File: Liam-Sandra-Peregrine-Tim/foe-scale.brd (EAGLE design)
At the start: 96.2 x 67.3 mm, 49 parts, among them U1 LM311, U2 SAMD21E

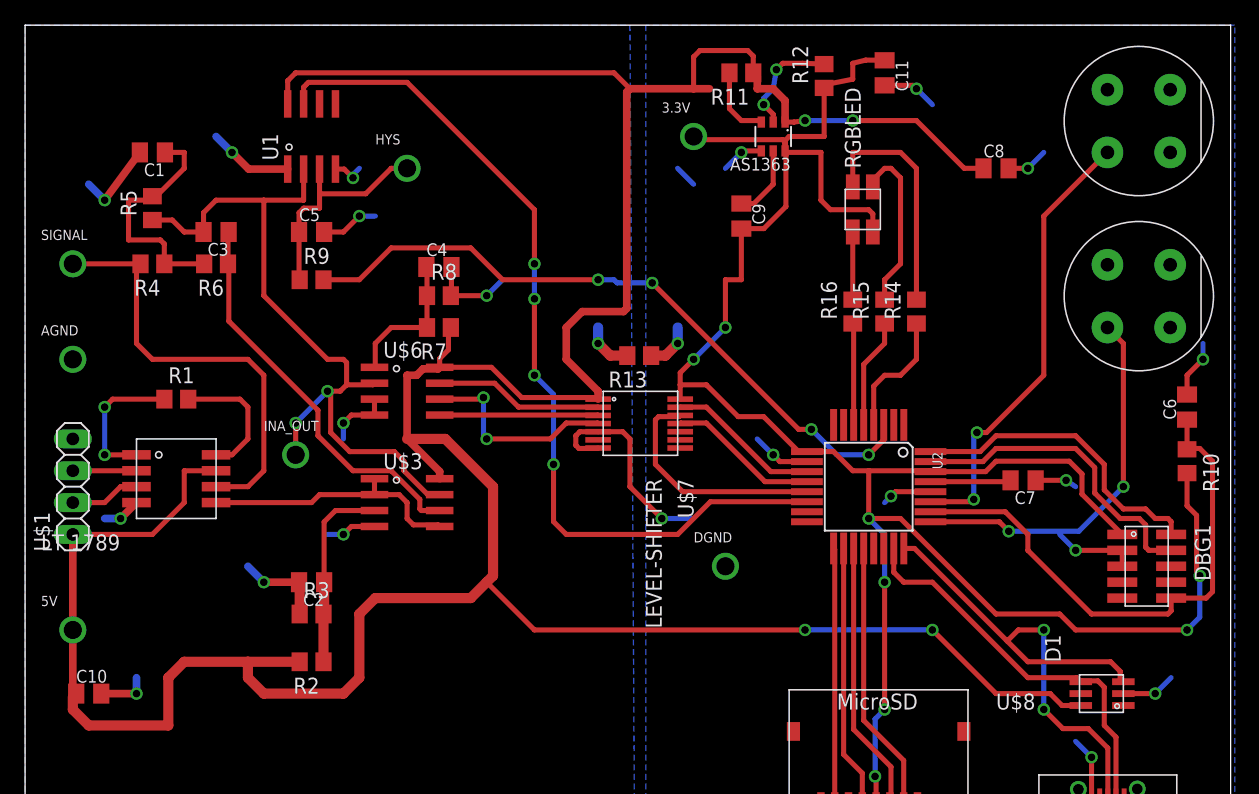
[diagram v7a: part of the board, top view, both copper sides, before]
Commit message: committing in addition to saving because fck Eagle
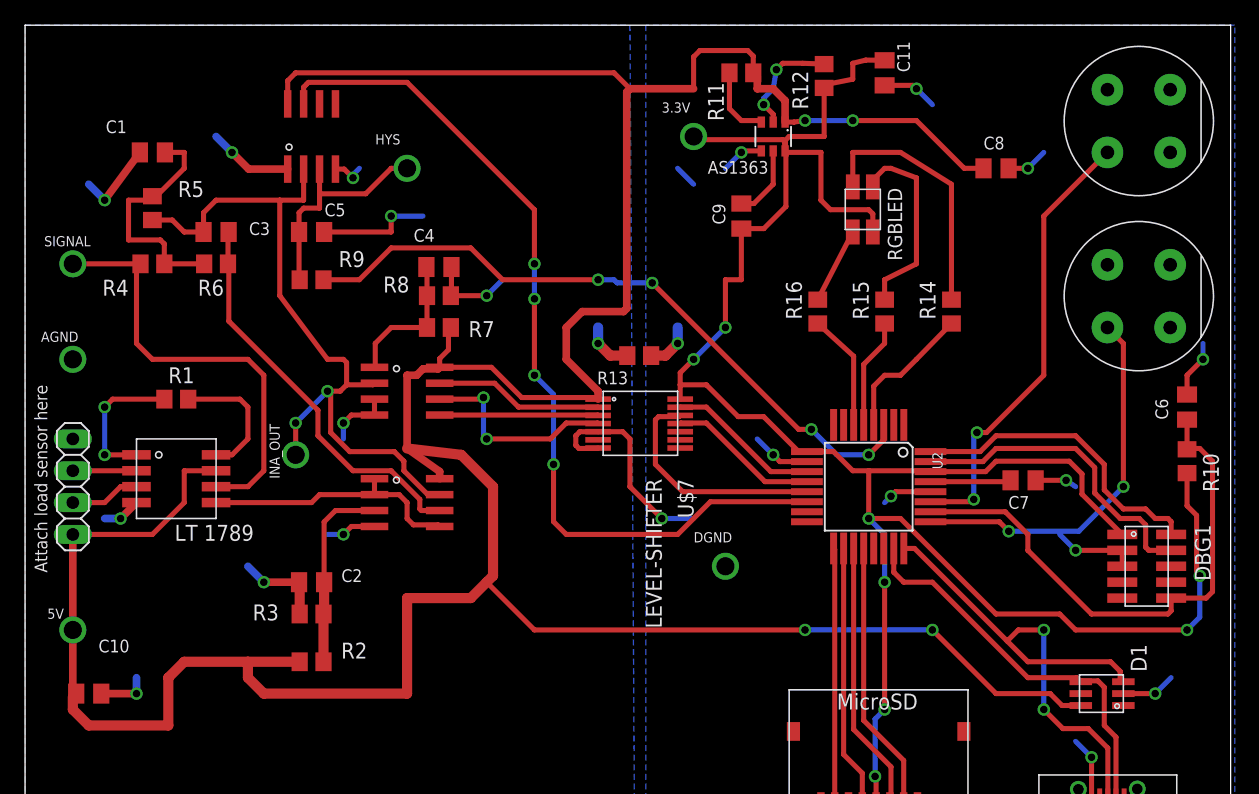
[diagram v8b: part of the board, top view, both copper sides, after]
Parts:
- moved R14 2.79 mm to (80.3, 57.1)
- moved R16 2.79 mm to (69.6, 57.1)
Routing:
- net AGND: track 55.2 -> 59.7 mm
- net N$49: track 13.7 -> 15.8 mm
- net N$48: track 18.8 -> 20.6 mm
- net N$8: track 8.12 -> 9.36 mm
- net N$1: track 10.2 -> 11.4 mm
- net N$19: track 59.9 -> 59.0 mm
- net N$50: track 5.40 -> 6.08 mm
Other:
- board text added: "Attach load sensor here"
